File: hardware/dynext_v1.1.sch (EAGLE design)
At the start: 43 parts, among them IC1 TPS560200, IC2 LM4040D20IDBZT, J1 AVR_SPI_PRG_6PTH, P1 PIN_SMD_2X2.5, P2 PIN_SMD_2X2.5, U1 ATxmega16E5, U2 TLV70033DCK, U4 TXB0101DCK, U5 TXB0101DCK, X1 CRYSTAL-0500290P1

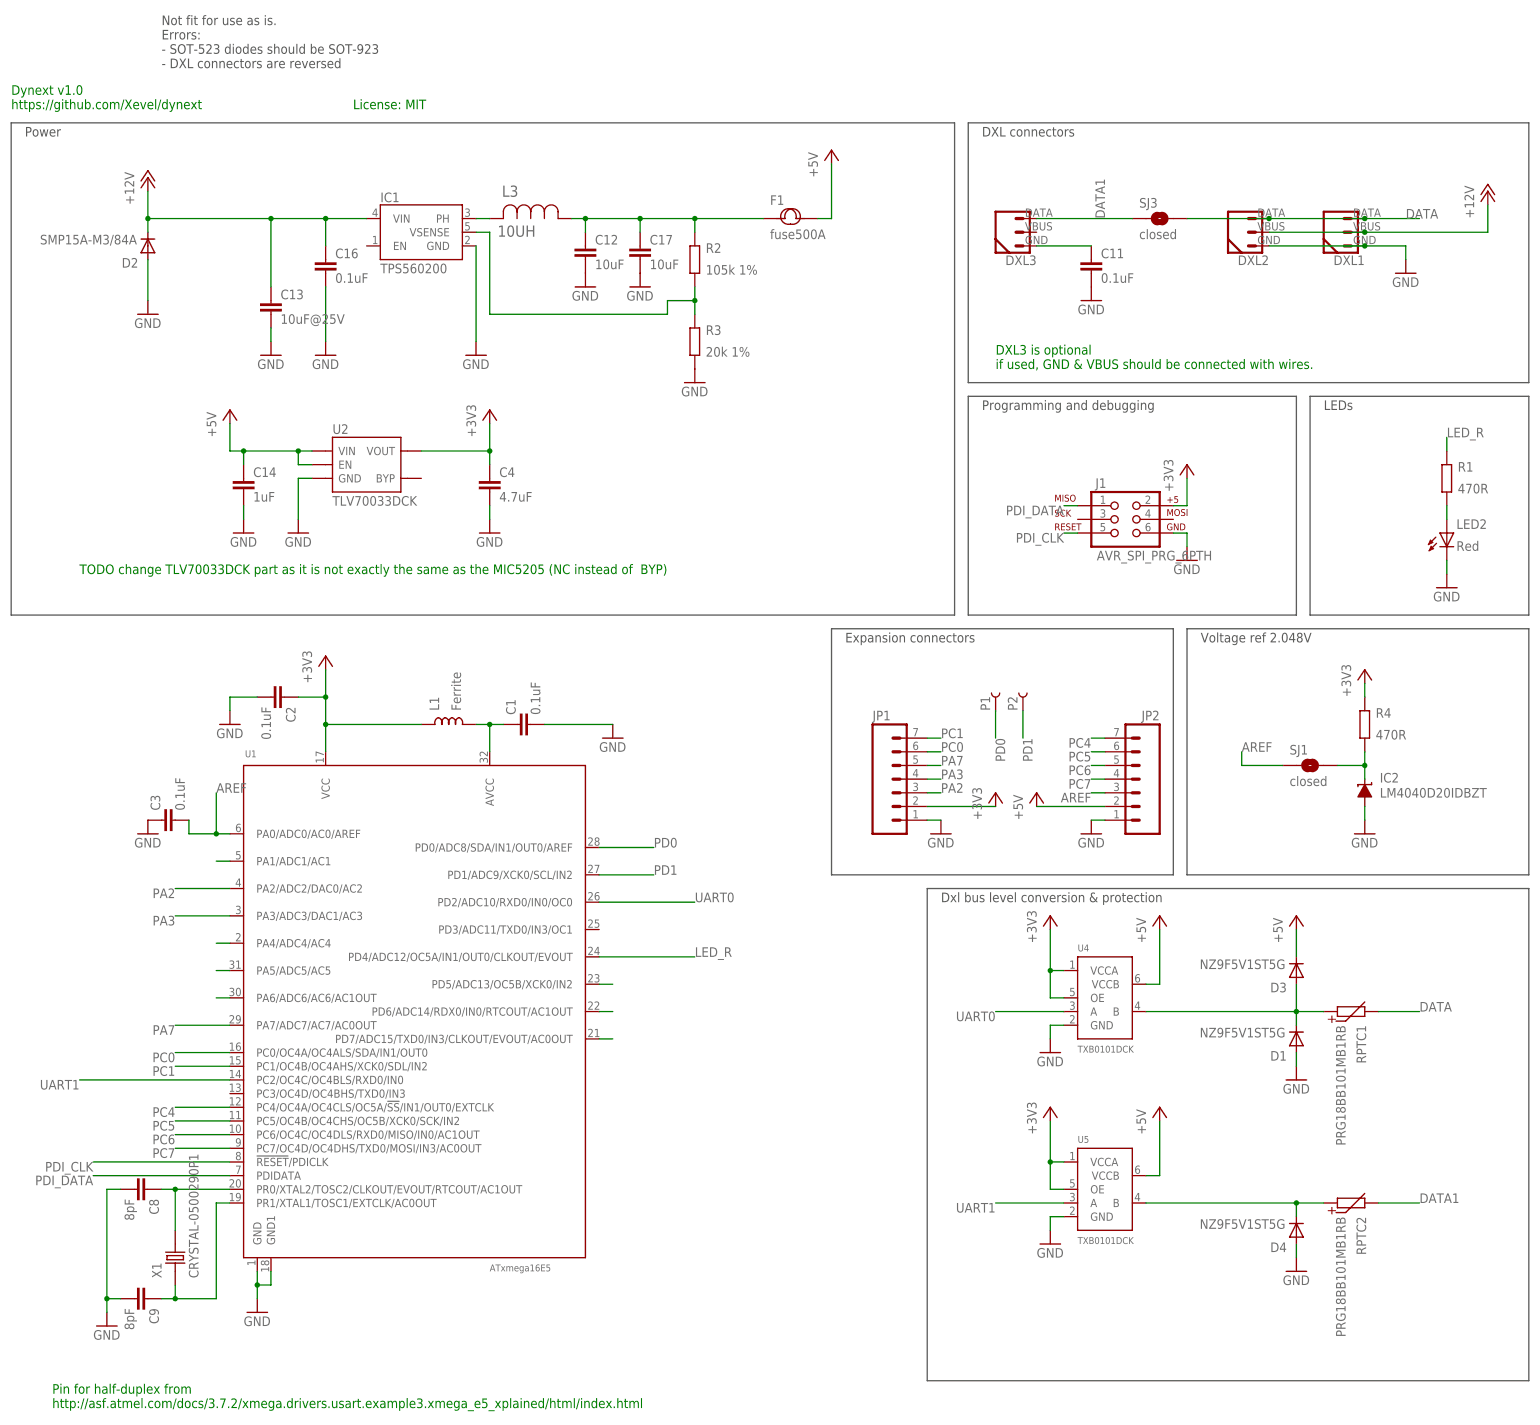
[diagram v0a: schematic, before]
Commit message: Cleanup of versions of the board. Added semi-corrected version of v1, it I ever want to go back to it...
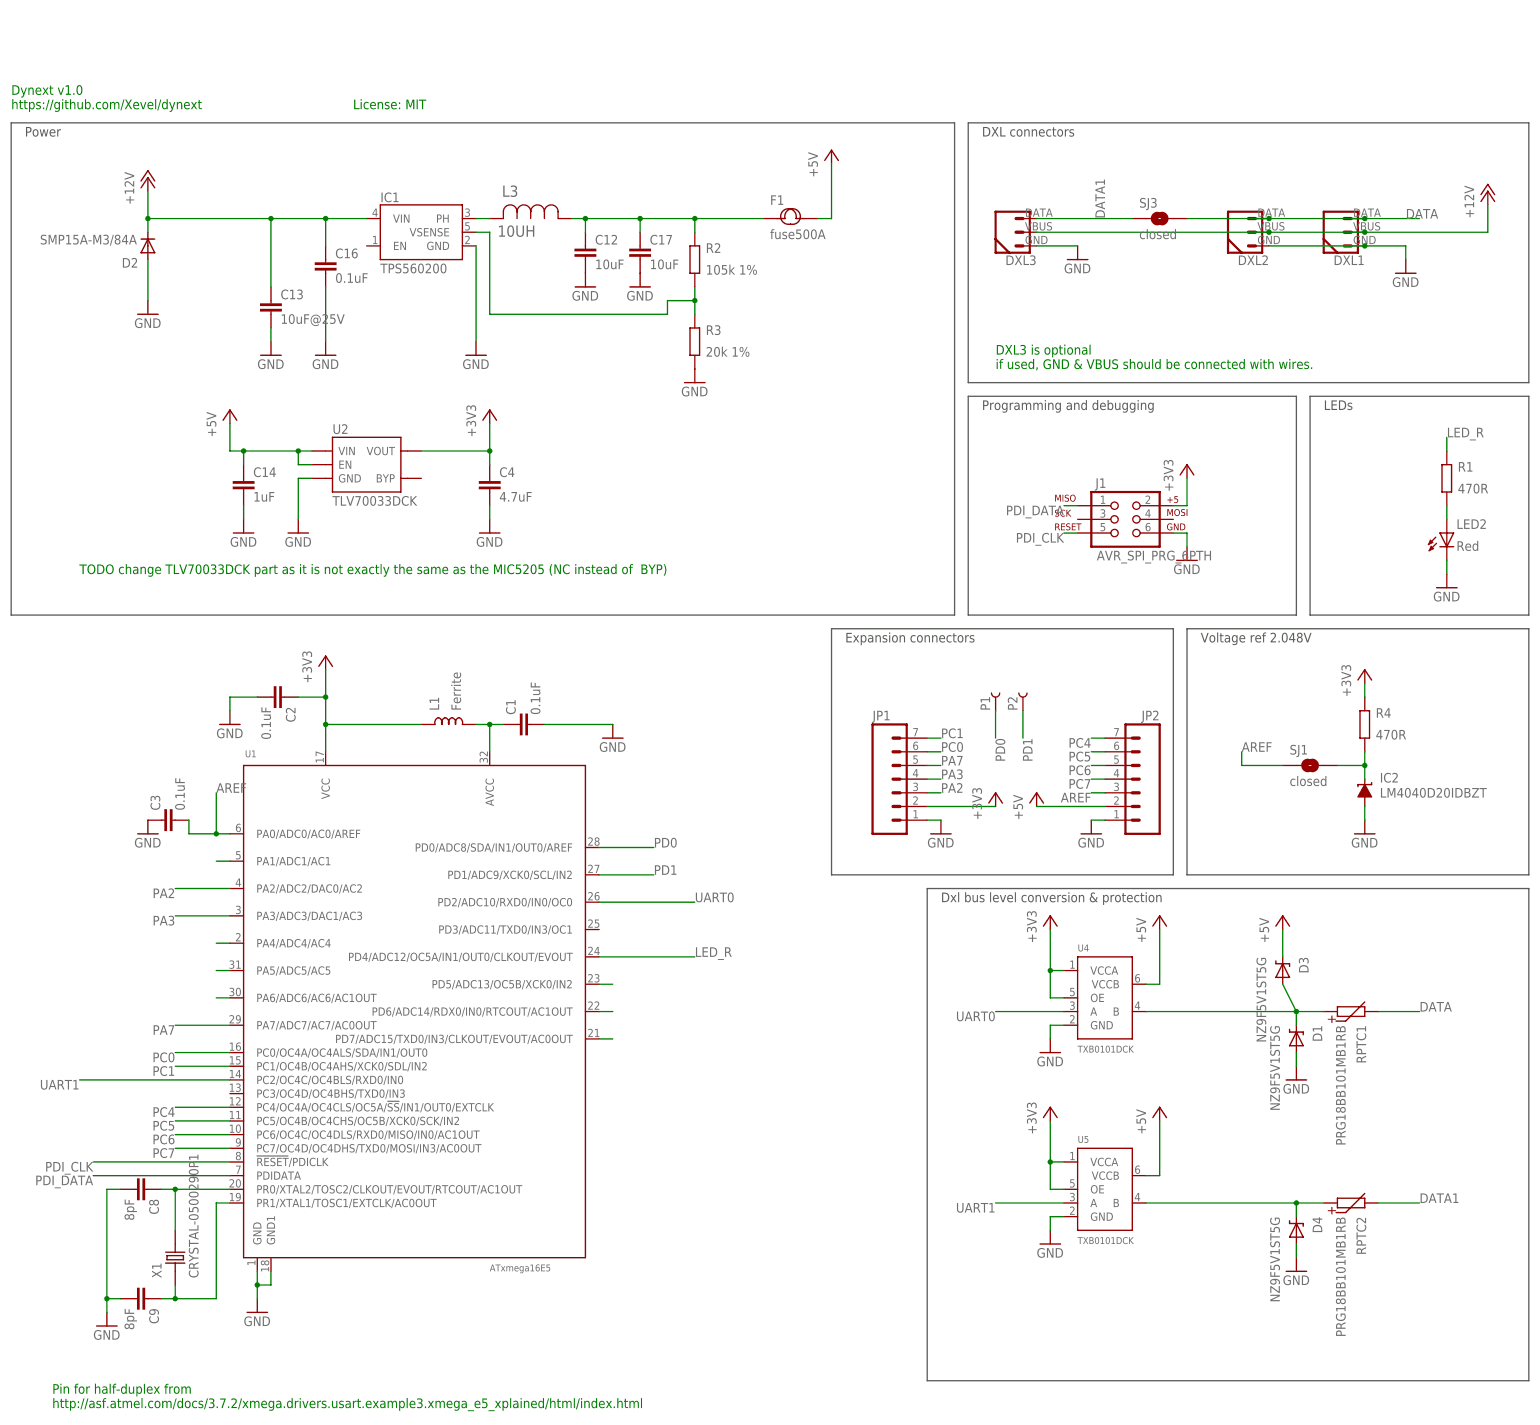
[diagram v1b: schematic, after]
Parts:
- removed C11: 0.1uF, Xevelabs:C0402
- D1, D3, D4: device Xevelabs:DIODE-SOD523 -> Xevelabs:DIODE_ZENER-923
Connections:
- removed net N$1: C11.1, DXL3.1
- net +12V: now also DXL3.2
- net GND: now also DXL3.1; no longer C11.2
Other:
- note removed: "Not fit for use as is. Errors: - SOT-523 diodes should be SOT-923 - DXL connectors are reversed"
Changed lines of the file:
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@@
 <part name="RPTC1" library="Xevelabs" deviceset="R-PTC" device="0603" value="PRG18BB101MB1RB "/>
 <part name="GND13" library="supply1" deviceset="GND" device=""/>
-<part name="D1" library="Xevelabs" deviceset="DIODE" device="-SOD523" value="NZ9F5V1ST5G"/>
-<part name="D3" library="Xevelabs" deviceset="DIODE" device="-SOD523" value="NZ9F5V1ST5G"/>
+<part name="D1" library="Xevelabs" deviceset="DIODE_ZENER" device="-923" value="NZ9F5V1ST5G"/>
+<part name="D3" library="Xevelabs" deviceset="DIODE_ZENER" device="-923" value="NZ9F5V1ST5G"/>
 <part name="P+6" library="supply1" deviceset="+5V" device=""/>
 <part name="GND14" library="supply1" deviceset="GND" device=""/>
@@
 <part name="RPTC2" library="Xevelabs" deviceset="R-PTC" device="0603" value="PRG18BB101MB1RB "/>
 <part name="GND19" library="supply1" deviceset="GND" device=""/>
-<part name="D4" library="Xevelabs" deviceset="DIODE" device="-SOD523" value="NZ9F5V1ST5G"/>
+<part name="D4" library="Xevelabs" deviceset="DIODE_ZENER" device="-923" value="NZ9F5V1ST5G"/>
 <part name="U5" library="MWquad_stuff" deviceset="TXB0101" device="DCK"/>
 <part name="GND20" library="supply1" deviceset="GND" device=""/>
@@
 <part name="L3" library="Panasonic-ELL" deviceset="ELL" device="-4XG" technology="4LG100MA" value=" 10UH "/>
 <part name="R1" library="Xevelabs" deviceset="R" device="0402" value="470R"/>
-<part name="C11" library="Xevelabs" deviceset="C" device="0402" value="0.1uF"/>
 <part name="GND22" library="supply1" deviceset="GND" device=""/>
 <part name="IC2" library="texas" deviceset="LM4041" device="DBZ" technology="A12" value="LM4040D20IDBZT"/>
@@
 https://github.com/Xevel/dynext</text>
 <text x="60.96" y="243.84" size="1.778" layer="91">License: MIT</text>
-<text x="25.4" y="251.46" size="1.778" layer="92">Not fit for use as is.
-Errors:
-- SOT-523 diodes should be SOT-923
-- DXL connectors are reversed</text>
 </plain>
 <instances>
@@
 <instance part="GND13" gate="1" x="236.22" y="63.5"/>
 <instance part="D1" gate="G$1" x="236.22" y="71.12" rot="R180"/>
-<instance part="D3" gate="G$1" x="236.22" y="83.82" rot="R180"/>
-<instance part="P+6" gate="1" x="236.22" y="93.98"/>
+<instance part="D3" gate="G$1" x="233.68" y="83.82" rot="R180"/>
+<instance part="P+6" gate="1" x="233.68" y="93.98"/>
 <instance part="GND14" gate="1" x="55.88" y="198.12"/>
 <instance part="GND16" gate="1" x="124.46" y="193.04"/>
@@
 <instance part="L3" gate="A" x="86.36" y="223.52"/>
 <instance part="R1" gate="G$1" x="264.16" y="175.26"/>
-<instance part="C11" gate="G$1" x="198.12" y="213.36"/>
-<instance part="GND22" gate="1" x="198.12" y="208.28"/>
+<instance part="GND22" gate="1" x="195.58" y="215.9"/>
 <instance part="IC2" gate="G$1" x="248.92" y="116.84"/>
 <instance part="R4" gate="G$1" x="248.92" y="129.54"/>
@@
 </segment>
 <segment>
-<pinref part="C11" gate="G$1" pin="2"/>
-<pinref part="GND22" gate="1" pin="GND"/>
-</segment>
-<segment>
 <pinref part="GND6" gate="1" pin="GND"/>
 <pinref part="JP1" gate="G$1" pin="1"/>
@@
 <pinref part="GND27" gate="1" pin="GND"/>
 <wire x1="248.92" y1="114.3" x2="248.92" y2="111.76" width="0.1524" layer="91"/>
+</segment>
+<segment>
+<wire x1="187.96" y1="218.44" x2="195.58" y2="218.44" width="0.1524" layer="91"/>
+<pinref part="DXL3" gate="G$1" pin="1"/>
+<pinref part="GND22" gate="1" pin="GND"/>
 </segment>
 </net>
@@
 <pinref part="P+4" gate="1" pin="+12V"/>
 <junction x="248.92" y="220.98"/>
+<pinref part="DXL3" gate="G$1" pin="2"/>
+<wire x1="187.96" y1="220.98" x2="231.14" y2="220.98" width="0.1524" layer="91"/>
+<junction x="231.14" y="220.98"/>
 </segment>
 </net>
@@
 <pinref part="D3" gate="G$1" pin="C"/>
 <pinref part="P+6" gate="1" pin="+5V"/>
-<wire x1="236.22" y1="86.36" x2="236.22" y2="91.44" width="0.1524" layer="91"/>
+<wire x1="233.68" y1="86.36" x2="233.68" y2="91.44" width="0.1524" layer="91"/>
 </segment>
 <segment>
@@
 <pinref part="D1" gate="G$1" pin="C"/>
 <pinref part="D3" gate="G$1" pin="A"/>
-<wire x1="236.22" y1="76.2" x2="236.22" y2="81.28" width="0.1524" layer="91"/>
+<wire x1="236.22" y1="76.2" x2="233.68" y2="81.28" width="0.1524" layer="91"/>
 <pinref part="U4" gate="G$1" pin="B"/>
 <wire x1="208.28" y1="76.2" x2="236.22" y2="76.2" width="0.1524" layer="91"/>
@@
 </segment>
 </net>
-<net name="N$1" class="0">
-<segment>
-<pinref part="C11" gate="G$1" pin="1"/>
-<wire x1="187.96" y1="218.44" x2="198.12" y2="218.44" width="0.1524" layer="91"/>
-<pinref part="DXL3" gate="G$1" pin="1"/>
-</segment>
-</net>
